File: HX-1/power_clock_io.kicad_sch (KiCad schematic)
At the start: 30 parts, among them J2 Conn_01x02_Socket, J5 3V3_Out, J6 5V_Out, U3 XC6206P332MR-G, Y1 16MHz

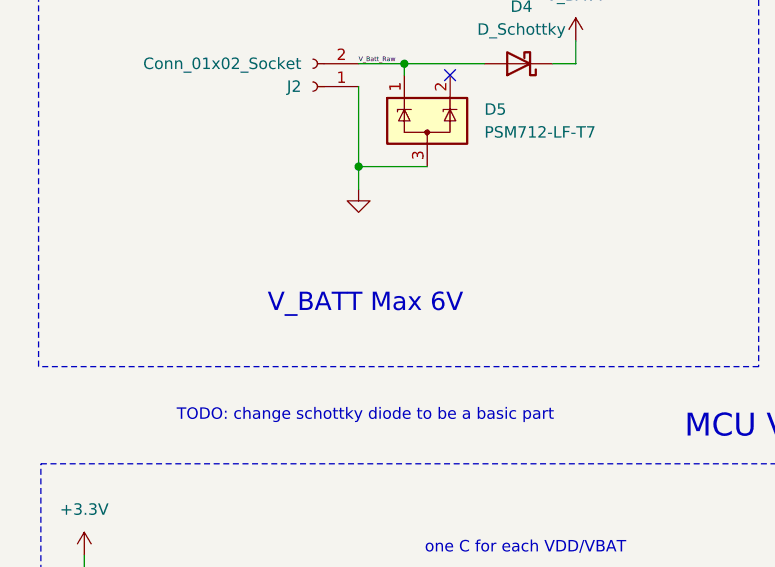
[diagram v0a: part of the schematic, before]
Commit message: update scripts to export pcb svg
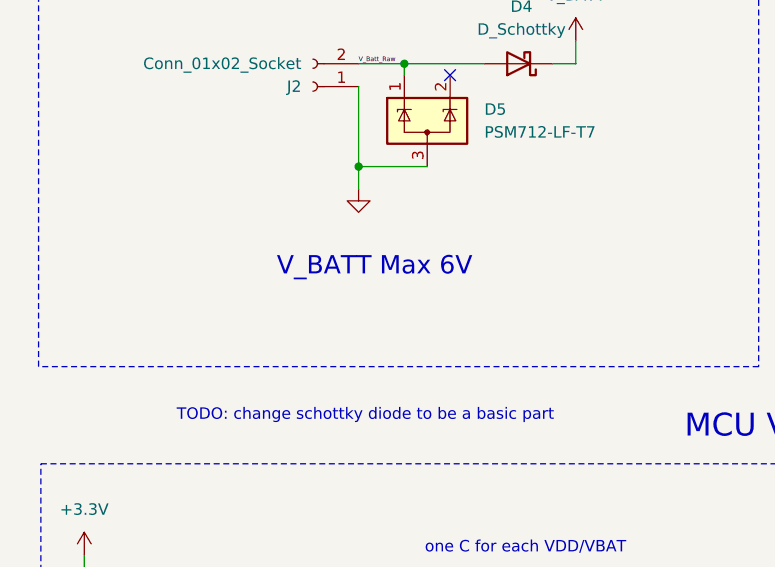
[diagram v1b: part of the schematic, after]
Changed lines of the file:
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@@
 	(text "V_BATT Max 6V"
 		(exclude_from_sim no)
-		(at 52.832 68.58 0)
+		(at 53.848 64.516 0)
 		(effects
 			(font

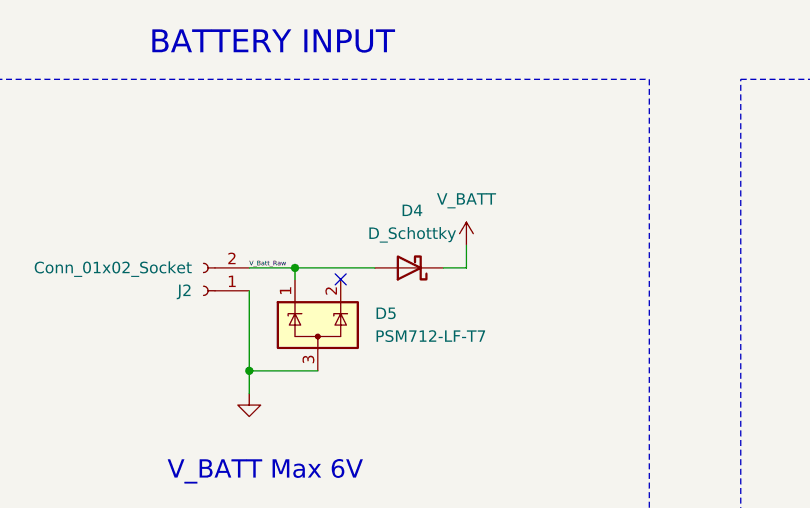
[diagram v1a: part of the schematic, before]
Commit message: change schottky diode to basic part from jlcpcb
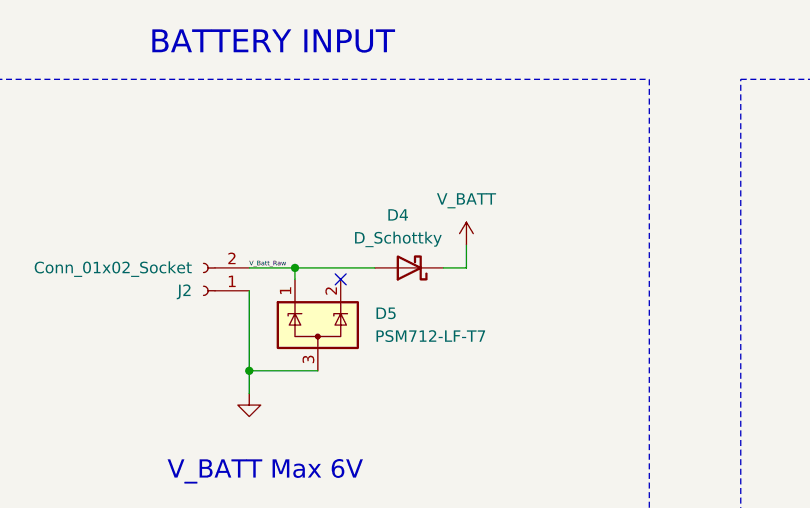
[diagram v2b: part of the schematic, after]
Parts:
- D4: footprint Diode_SMD:D_SOD-323F -> Diode_SMD:D_SOD-323; LCSC PN C146335 -> C191023
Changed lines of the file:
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@@
+	)
+	(symbol
+		(lib_id "Device:D_Schottky")
+		(at 69.85 41.91 180)
+		(unit 1)
+		(exclude_from_sim no)
+		(in_bom yes)
+		(on_board yes)
+		(dnp no)
+		(property "Reference" "D4"
+			(at 68.58 36.068 0)
+			(effects
+				(font
+					(size 1.27 1.27)
+				)
+			)
+		)
+		(property "Value" "D_Schottky"
+			(at 68.58 38.608 0)
+			(effects
+				(font
+					(size 1.27 1.27)
+				)
+			)
+		)
+		(property "Footprint" "Diode_SMD:D_SOD-323"
+			(at 69.85 41.91 0)
+			(effects
+				(font
+					(size 1.27 1.27)
+				)
+				(hide yes)
+			)
+		)
+		(property "Datasheet" "~"
+			(at 69.85 41.91 0)
+			(effects
+				(font
+					(size 1.27 1.27)
+				)
+				(hide yes)
+			)
+		)
+		(property "Description" "Schottky diode"
+			(at 69.85 41.91 0)
+			(effects
+				(font
+					(size 1.27 1.27)
+				)
+				(hide yes)
+			)
+		)
+		(property "LCSC PN" "C191023"
+			(at 69.85 41.91 90)
+			(effects
+				(font
+					(size 1.27 1.27)
+				)
+				(hide yes)
+			)
+		)
+		(pin "1"
+		)
+		(pin "2"
+		)
+		(instances
+			(project "HX-1"
+				(path "/a3219989-2bf1-44ea-9412-fab86edfb39b/3a90d823-0fb3-4447-b918-f2095473f7ca"
+					(reference "D4")
+					(unit 1)
+				)
+			)
+		)
 	)
 	(symbol
@@
 					(unit 1)
 				)
-			)
-		)
-	)
-	(symbol
-		(lib_id "Device:D_Schottky")
-		(at 69.85 41.91 180)
-		(unit 1)
-		(exclude_from_sim no)
-		(in_bom yes)
-		(on_board yes)
-		(dnp no)
-		(fields_autoplaced yes)
-		(property "Reference" "D4"
-			(at 70.1675 35.56 0)
-			(effects
-				(font
-					(size 1.27 1.27)
-				)
-			)
-		)
-		(property "Value" "D_Schottky"
-			(at 70.1675 38.1 0)
-			(effects
-				(font
-					(size 1.27 1.27)
-				)
-			)
-		)
-		(property "Footprint" "Diode_SMD:D_SOD-323F"
-			(at 69.85 41.91 0)
-			(effects
-				(font
-					(size 1.27 1.27)
-				)
-				(hide yes)
-			)
-		)
-		(property "Datasheet" "~"
-			(at 69.85 41.91 0)
-			(effects
-				(font
-					(size 1.27 1.27)
-				)
-				(hide yes)
-			)
-		)
-		(property "Description" "Schottky diode"
-			(at 69.85 41.91 0)
-			(effects
-				(font
-					(size 1.27 1.27)
-				)
-				(hide yes)
-			)
-		)
-		(property "LCSC PN" "C146335"
-			(at 69.85 41.91 90)
-			(effects
-				(font
-					(size 1.27 1.27)
-				)
-				(hide yes)
-			)
-		)
-		(pin "1"
-		)
-		(pin "2"
-		)
-		(instances
-			(project "HX-1"
-				(path "/a3219989-2bf1-44ea-9412-fab86edfb39b/3a90d823-0fb3-4447-b918-f2095473f7ca"
-					(reference "D4")
-					(unit 1)
-				)

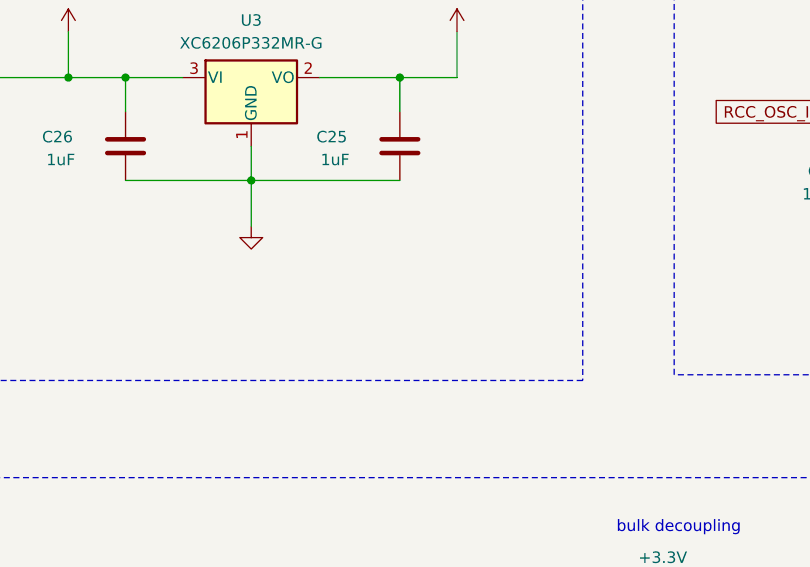
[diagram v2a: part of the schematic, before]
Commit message: add 3v3 led and pwm led, position mounting holes and pin header
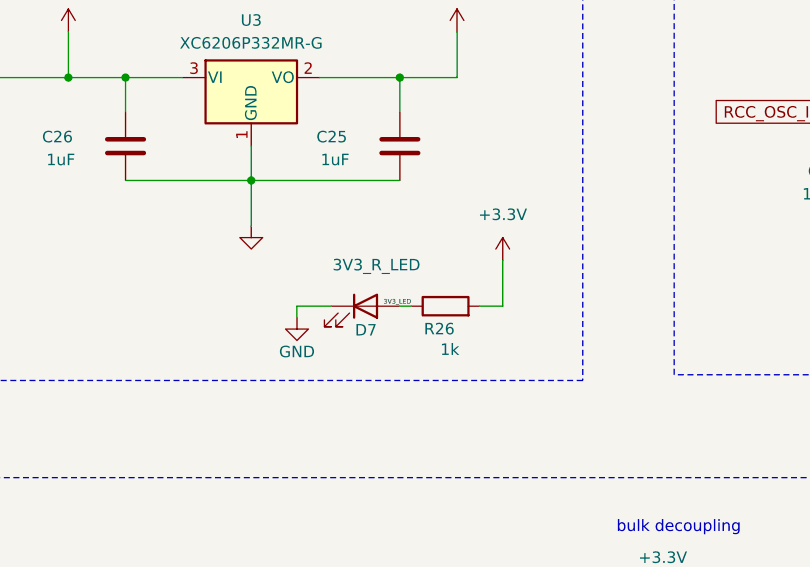
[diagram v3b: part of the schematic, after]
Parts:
- added D7: 3V3_R_LED, LED_SMD:LED_0603_1608Metric, symbol Device:LED
- added R26: 1k, Resistor_SMD:R_0603_1608Metric, symbol Device:R
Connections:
- net +3.3V: now also R26.2
- net GND: now also D7.1 (K)
- new net 3V3_LED: D7.2 (A), R26.1

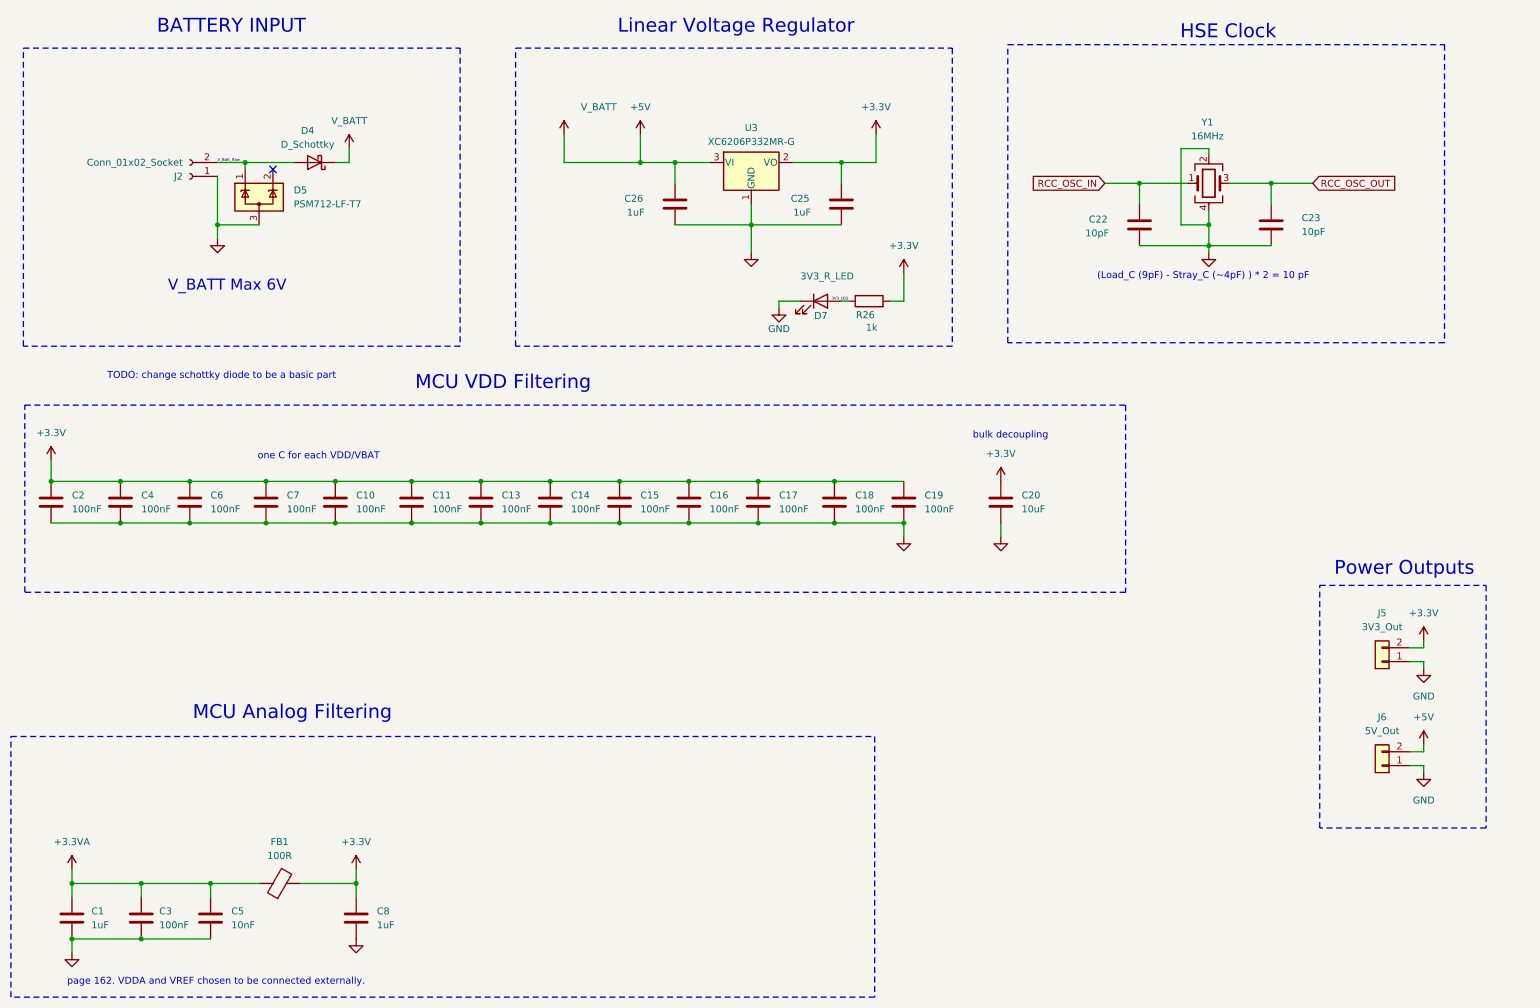
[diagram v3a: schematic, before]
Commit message: clean up schematic, layout more of pcb, fix some footprints
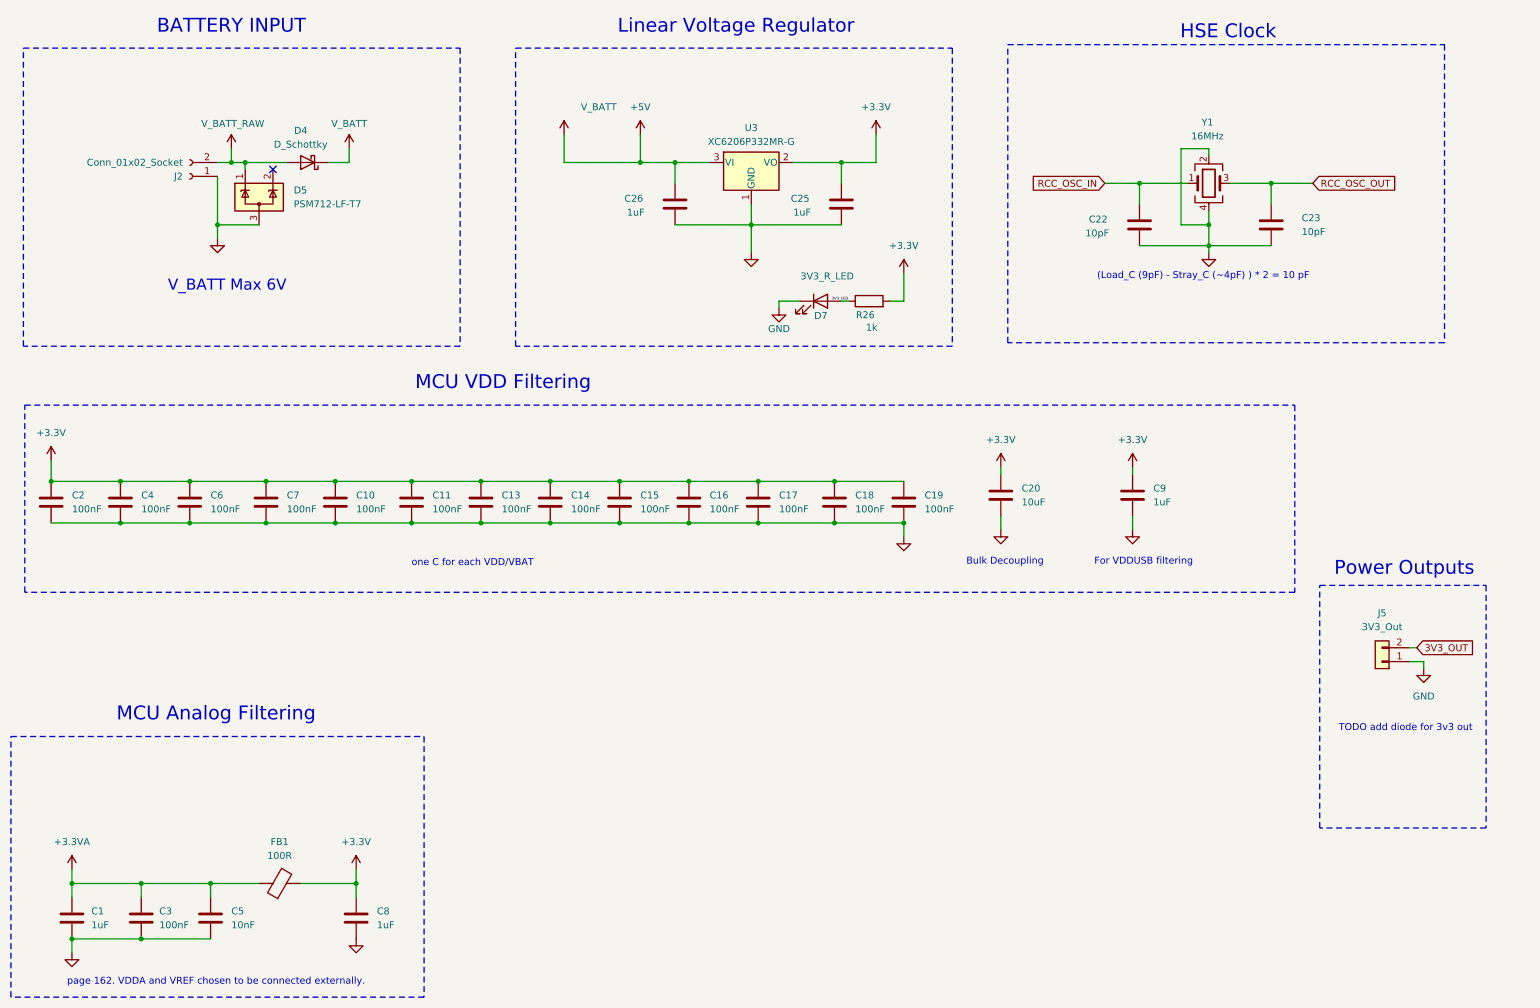
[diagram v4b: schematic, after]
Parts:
- removed J6: 5V_Out, symbol Connector_Generic:Conn_01x02
- added C9: 1uF, Capacitor_SMD:C_0603_1608Metric, symbol Device:C
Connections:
- net +3.3V: now also C9.1; no longer J5.2 (Pin_2)
- net GND: now also C9.2
- net V_Batt_Raw renamed V_BATT_RAW
- new net 3V3_OUT: J5.2 (Pin_2)
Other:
- note added: "Bulk Decoupling"
- note added: "For VDDUSB filtering"
- note added: "TODO add diode for 3v3 out"
- note removed: "TODO: change schottky diode to be a basic part"
- note removed: "bulk decoupling"
- moved on the sheet: C20, D4

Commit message: renumber capacitors, position all MCU caps
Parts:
- renumbered C2 to C1, C16 to C10, C17 to C11, C18 to C12, C19 to C13, C20 to C14, C9 to C15, C1 to C16, C3 to C17, C5 to C18, C8 to C19, C4 to C2, C26 to C20, C25 to C21, C6 to C3, C7 to C4, C10 to C5, C11 to C6, C13 to C7, C14 to C8, C15 to C9
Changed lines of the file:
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@@
 		(dnp no)
 		(fields_autoplaced yes)
-		(property "Reference" "C18"
+		(property "Reference" "C12"
 			(at 168.91 102.8699 0)
 			(effects
@@
 			(project "HX-1"
 				(path "/a3219989-2bf1-44ea-9412-fab86edfb39b/3a90d823-0fb3-4447-b918-f2095473f7ca"
-					(reference "C18")
+					(reference "C12")
 					(unit 1)
 				)
@@
 		(on_board yes)
 		(dnp no)
-		(property "Reference" "C1"
+		(property "Reference" "C16"
 			(at 28.956 179.07 0)
 			(effects
@@
 			(project "HX-1"
 				(path "/a3219989-2bf1-44ea-9412-fab86edfb39b/3a90d823-0fb3-4447-b918-f2095473f7ca"
-					(reference "C1")
+					(reference "C16")
 					(unit 1)
 				)
@@
 		(dnp no)
 		(fields_autoplaced yes)
-		(property "Reference" "C6"
+		(property "Reference" "C3"
 			(at 50.8 102.8699 0)
 			(effects
@@
 			(project "HX-1"
 				(path "/a3219989-2bf1-44ea-9412-fab86edfb39b/3a90d823-0fb3-4447-b918-f2095473f7ca"
-					(reference "C6")
+					(reference "C3")
 					(unit 1)
 				)
@@
 		(dnp no)
 		(fields_autoplaced yes)
-		(property "Reference" "C7"
+		(property "Reference" "C4"
 			(at 64.77 102.8699 0)
 			(effects
@@
 			(project "HX-1"
 				(path "/a3219989-2bf1-44ea-9412-fab86edfb39b/3a90d823-0fb3-4447-b918-f2095473f7ca"
-					(reference "C7")
+					(reference "C4")
 					(unit 1)
 				)
@@
 		(dnp no)
 		(fields_autoplaced yes)
-		(property "Reference" "C11"
+		(property "Reference" "C6"
 			(at 91.44 102.8699 0)
 			(effects
@@
 			(project "HX-1"
 				(path "/a3219989-2bf1-44ea-9412-fab86edfb39b/3a90d823-0fb3-4447-b918-f2095473f7ca"
-					(reference "C11")
+					(reference "C6")
 					(unit 1)
 				)
@@
 		(dnp no)
 		(fields_autoplaced yes)
-		(property "Reference" "C15"
+		(property "Reference" "C9"
 			(at 129.54 102.8699 0)
 			(effects
@@
 			(project "HX-1"
 				(path "/a3219989-2bf1-44ea-9412-fab86edfb39b/3a90d823-0fb3-4447-b918-f2095473f7ca"
-					(reference "C15")
+					(reference "C9")
 					(unit 1)
 				)
@@
 		(on_board yes)
 		(dnp no)
-		(property "Reference" "C3"
+		(property "Reference" "C17"
 			(at 41.402 179.07 0)
 			(effects
@@
 			(project "HX-1"
 				(path "/a3219989-2bf1-44ea-9412-fab86edfb39b/3a90d823-0fb3-4447-b918-f2095473f7ca"
-					(reference "C3")
+					(reference "C17")
 					(unit 1)
 				)
@@
 		(dnp no)
 		(fields_autoplaced yes)
-		(property "Reference" "C5"
+		(property "Reference" "C18"
 			(at 54.61 179.0699 0)
 			(effects
@@
 			(project "HX-1"
 				(path "/a3219989-2bf1-44ea-9412-fab86edfb39b/3a90d823-0fb3-4447-b918-f2095473f7ca"
-					(reference "C5")
+					(reference "C18")
 					(unit 1)
 				)
@@
 		(dnp no)
 		(fields_autoplaced yes)
-		(property "Reference" "C20"
+		(property "Reference" "C14"
 			(at 199.39 101.5999 0)
 			(effects
@@
 			(project "HX-1"
 				(path "/a3219989-2bf1-44ea-9412-fab86edfb39b/3a90d823-0fb3-4447-b918-f2095473f7ca"
-					(reference "C20")
+					(reference "C14")
 					(unit 1)
 				)
@@
 		(dnp no)
 		(fields_autoplaced yes)
-		(property "Reference" "C2"
+		(property "Reference" "C1"
 			(at 25.4 102.8699 0)
 			(effects
@@
 			(project "HX-1"
 				(path "/a3219989-2bf1-44ea-9412-fab86edfb39b/3a90d823-0fb3-4447-b918-f2095473f7ca"
-					(reference "C2")
+					(reference "C1")
 					(unit 1)
 				)
@@
 		(on_board yes)
 		(dnp no)
-		(property "Reference" "C9"
+		(property "Reference" "C15"
 			(at 223.52 101.5999 0)
 			(effects
@@
 			(project "HX-1"
 				(path "/a3219989-2bf1-44ea-9412-fab86edfb39b/3a90d823-0fb3-4447-b918-f2095473f7ca"
-					(reference "C9")
+					(reference "C15")
 					(unit 1)
 				)
@@
 		(dnp no)
 		(fields_autoplaced yes)
-		(property "Reference" "C4"
+		(property "Reference" "C2"
 			(at 38.1 102.8699 0)
 			(effects
@@
 			(project "HX-1"
 				(path "/a3219989-2bf1-44ea-9412-fab86edfb39b/3a90d823-0fb3-4447-b918-f2095473f7ca"
-					(reference "C4")
+					(reference "C2")
 					(unit 1)
 				)
@@
 		(on_board yes)
 		(dnp no)
-		(property "Reference" "C26"
+		(property "Reference" "C20"
 			(at 130.048 48.514 0)
 			(effects
@@
 			(project "HX-1"
 				(path "/a3219989-2bf1-44ea-9412-fab86edfb39b/3a90d823-0fb3-4447-b918-f2095473f7ca"
-					(reference "C26")
+					(reference "C20")
 					(unit 1)
 				)
@@
 		(on_board yes)
 		(dnp no)
-		(property "Reference" "C25"
+		(property "Reference" "C21"
 			(at 160.528 48.514 0)
 			(effects
@@
 			(project "HX-1"
 				(path "/a3219989-2bf1-44ea-9412-fab86edfb39b/3a90d823-0fb3-4447-b918-f2095473f7ca"
-					(reference "C25")
+					(reference "C21")
 					(unit 1)
 				)
@@
 		(dnp no)
 		(fields_autoplaced yes)
-		(property "Reference" "C14"
+		(property "Reference" "C8"
 			(at 116.84 102.8699 0)
 			(effects
@@
 			(project "HX-1"
 				(path "/a3219989-2bf1-44ea-9412-fab86edfb39b/3a90d823-0fb3-4447-b918-f2095473f7ca"
-					(reference "C14")
+					(reference "C8")
 					(unit 1)
 				)
@@
 		(dnp no)
 		(fields_autoplaced yes)
-		(property "Reference" "C16"
+		(property "Reference" "C10"
 			(at 142.24 102.8699 0)
 			(effects
@@
 			(project "HX-1"
 				(path "/a3219989-2bf1-44ea-9412-fab86edfb39b/3a90d823-0fb3-4447-b918-f2095473f7ca"
-					(reference "C16")
+					(reference "C10")
 					(unit 1)
 				)
@@
 		(dnp no)
 		(fields_autoplaced yes)
-		(property "Reference" "C17"
+		(property "Reference" "C11"
 			(at 154.94 102.8699 0)
 			(effects
@@
 			(project "HX-1"
 				(path "/a3219989-2bf1-44ea-9412-fab86edfb39b/3a90d823-0fb3-4447-b918-f2095473f7ca"
-					(reference "C17")
+					(reference "C11")
 					(unit 1)
 				)
@@
 		(dnp no)
 		(fields_autoplaced yes)
-		(property "Reference" "C19"
+		(property "Reference" "C13"
 			(at 181.61 102.8699 0)
 			(effects
@@
 			(project "HX-1"
 				(path "/a3219989-2bf1-44ea-9412-fab86edfb39b/3a90d823-0fb3-4447-b918-f2095473f7ca"
-					(reference "C19")
+					(reference "C13")
 					(unit 1)
 				)
@@
 		(dnp no)
 		(fields_autoplaced yes)
-		(property "Reference" "C13"
+		(property "Reference" "C7"
 			(at 104.14 102.8699 0)
 			(effects
@@
 			(project "HX-1"
 				(path "/a3219989-2bf1-44ea-9412-fab86edfb39b/3a90d823-0fb3-4447-b918-f2095473f7ca"
-					(reference "C13")
+					(reference "C7")
 					(unit 1)
 				)
@@
 		(dnp no)
 		(fields_autoplaced yes)
-		(property "Reference" "C8"
+		(property "Reference" "C19"
 			(at 81.28 179.0699 0)
 			(effects
@@
 			(project "HX-1"
 				(path "/a3219989-2bf1-44ea-9412-fab86edfb39b/3a90d823-0fb3-4447-b918-f2095473f7ca"
-					(reference "C8")
+					(reference "C19")
 					(unit 1)
 				)
@@
 		(dnp no)
 		(fields_autoplaced yes)
-		(property "Reference" "C10"
+		(property "Reference" "C5"
 			(at 77.47 102.8699 0)
 			(effects
@@
 			(project "HX-1"
 				(path "/a3219989-2bf1-44ea-9412-fab86edfb39b/3a90d823-0fb3-4447-b918-f2095473f7ca"
-					(reference "C10")
+					(reference "C5")
 					(unit 1)
 				)
